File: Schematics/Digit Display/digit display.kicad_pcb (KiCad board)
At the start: 2 copper layers, 72.2 x 42.7 mm, 24 parts, among them J1 Conn_01x07

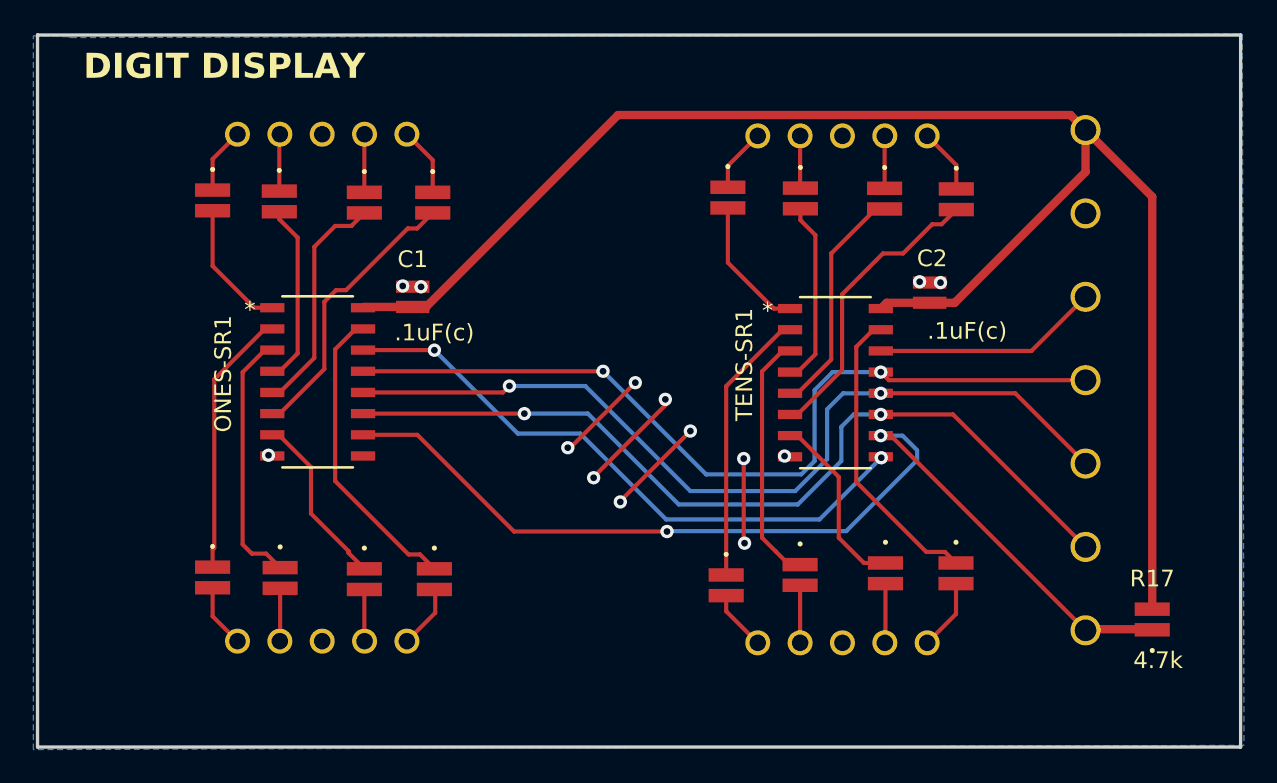
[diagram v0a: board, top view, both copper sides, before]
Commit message: updated schematic, layout and parts library
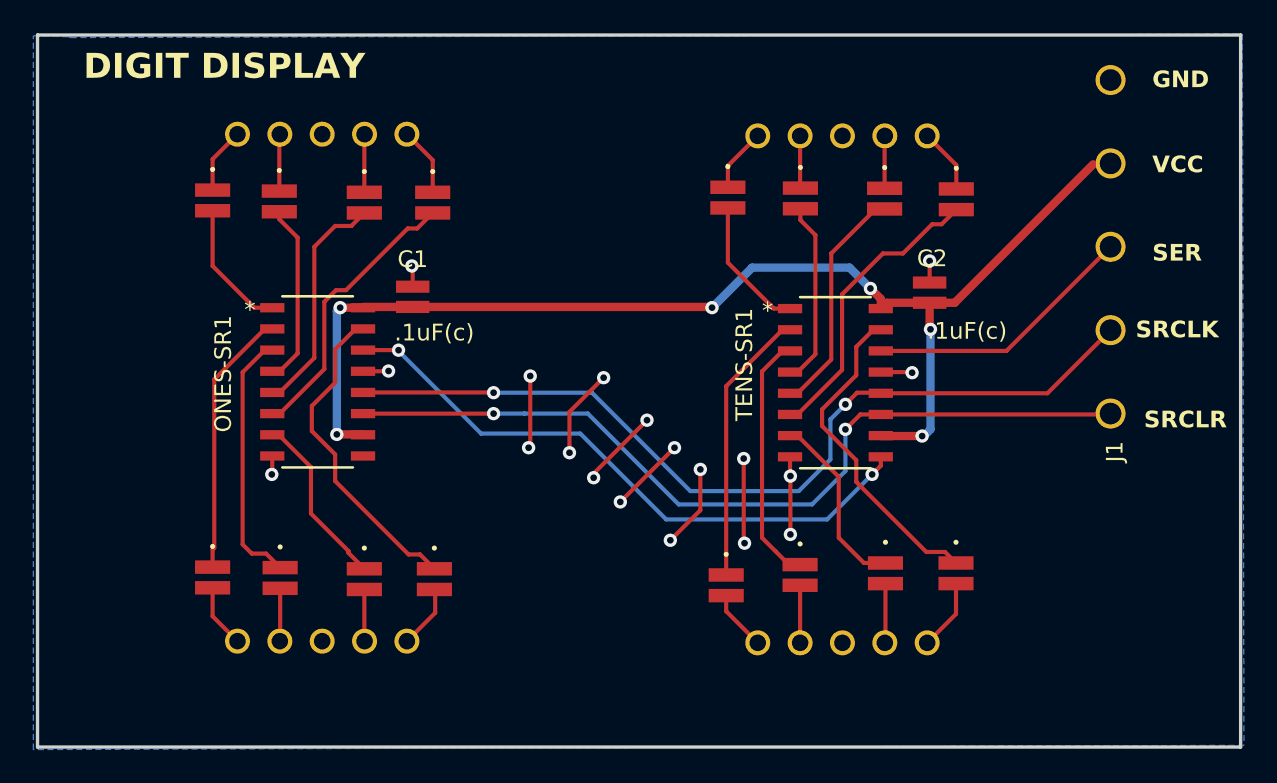
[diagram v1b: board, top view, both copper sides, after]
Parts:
- removed R17: 4.7k, pPSI:100ohm resistor
- J1: value Conn_01x07 -> 5-pin-header; footprint pPSI:7 pin header -> pPSI:5 pin header
- moved J1 13.1 mm to (84.0, 35.0)
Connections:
- J1 pad 1: /*SRCLR -> /SRCLK
- J1 pad 2: /SRCLK -> /RCLK
- J1 pad 3: /RCLK -> /SER
- J1 pad 4: /*OE -> /VCC
- J1 pad 5: /SER -> /GND
- ONES-SR1 pad 10: /*SRCLR -> /VCC
- ONES-SR1 pad 13: /*OE -> /GND
- TENS-SR1 pad 10: /*SRCLR -> /VCC
- TENS-SR1 pad 13: /*OE -> /GND
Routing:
- net /*SRCLR: track 61.7 -> 0.00 mm, vias 2 -> 0
- net /*OE: track 51.1 -> 0.00 mm, vias 2 -> 0
- net /VCC: track 97.1 -> 71.2 mm, vias 0 -> 6
- net /GND: track 23.4 -> 41.0 mm, vias 14 -> 19
- net /SER: track 13.6 -> 16.4 mm
- net /T7: track 18.0 -> 19.7 mm
- net /SRCLK: track 52.3 -> 50.8 mm
- net /O7: track 18.2 -> 19.4 mm
- net /RCLK: track 52.0 -> 52.7 mm
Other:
- board text removed: "*OE"
- board text removed: "RCLK"
